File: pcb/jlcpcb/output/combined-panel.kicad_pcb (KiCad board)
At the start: 2 copper layers, 138.8 x 150.1 mm, 163 parts, among them J101 B12B-PHDSS, J201 Conn_01x06_MountingPin, J202 B12B-PHDSS, SW10 SW_Push, SW11 SW_Push, SW12 SW_Push, SW13 SW_Push, SW15 SW_Push, SW16 SW_Push, SW17 SW_Push, SW18 SW_Push, SW19 SW_Push, SW20 SW_Push, SW22 SW_Push, SW23 SW_Push, SW24 SW_Push, SW25 SW_Push, SW26 SW_Push, SW27 SW_Push, SW28 SW_Push, SW29 SW_Push, SW30 SW_Push, SW31 SW_Push, SW32 SW_Push, SW33 SW_Push, SW34 SW_Push, SW35 SW_Push, SW43 SW_Push, SW44 SW_Push, SW45 SW_Push, SW46 SW_Push, SW47 SW_Push, SW48 SW_Push, SW50 SW_Push, SW51 SW_Push, SW52 SW_Push, SW53 SW_Push, SW54 SW_Push, SW55 SW_Push, SW57 SW_Push, SW58 SW_Push, SW59 SW_Push, SW60 SW_Push, SW61 SW_Push, SW62 SW_Push, SW63 SW_Push, SW64 SW_Push, SW65 SW_Push, SW69 SW_Push, SW70 SW_Push, SW8 SW_Push, SW9 SW_Push, U201 XIAO nRF52840 Plus

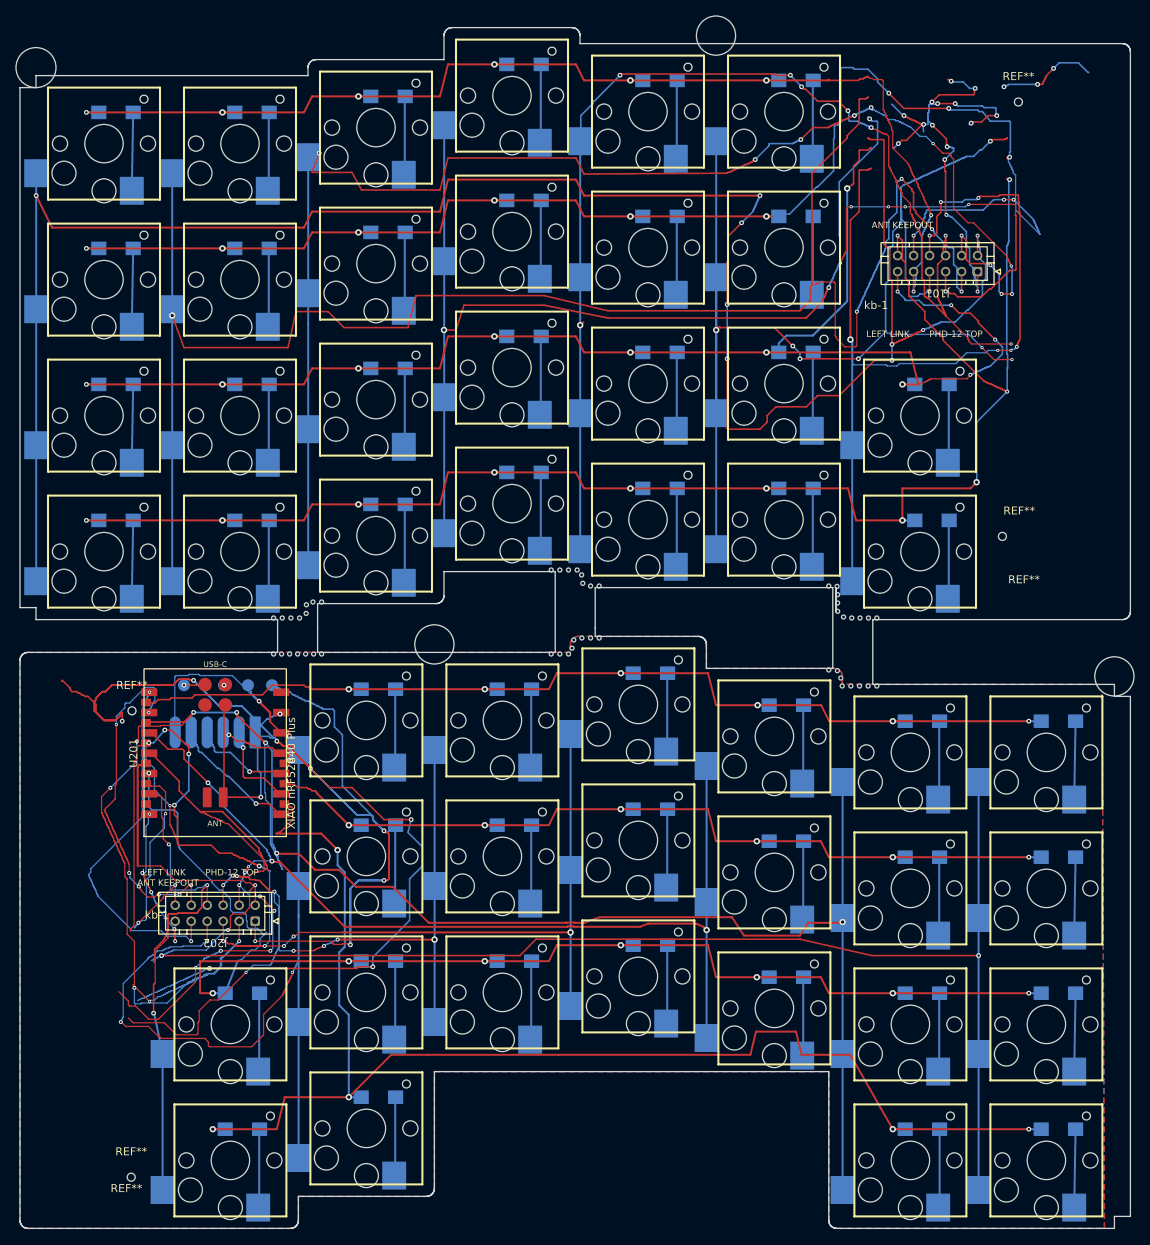
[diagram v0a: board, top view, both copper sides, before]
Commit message: Replace split connectors with Samtec FFSD-compatible headers
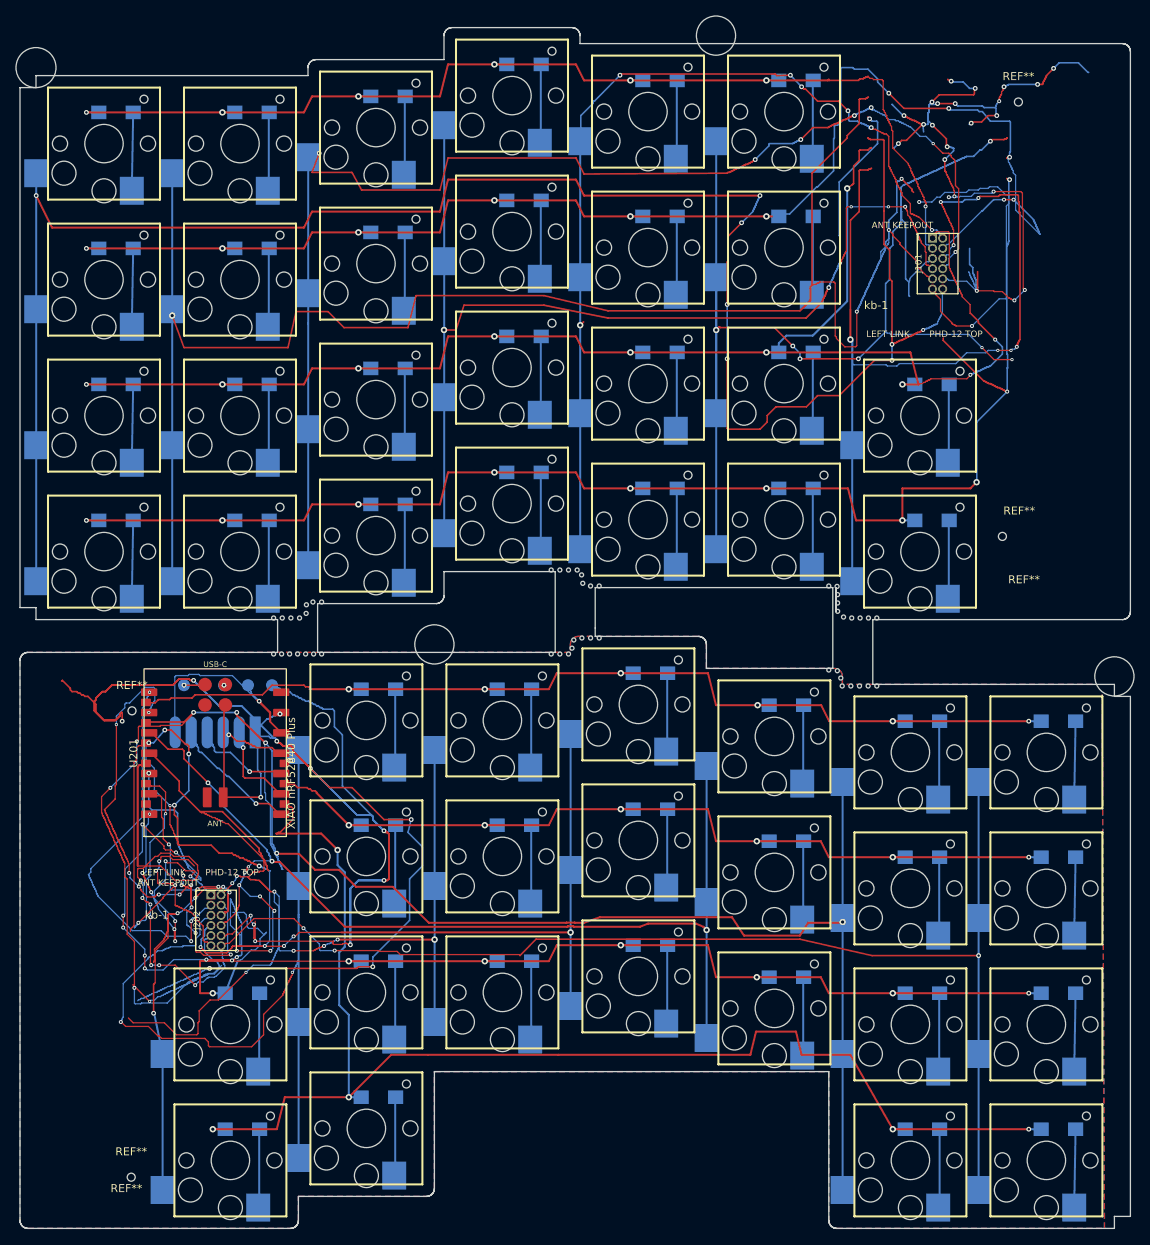
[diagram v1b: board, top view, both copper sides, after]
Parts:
- J101, J202: value B12B-PHDSS -> FTSH-106-01-L-D-K; footprint Connector_JST:JST_PHD_B12B-PHDSS_2x06_P2.00mm_Vertical -> Library:Samtec_FTSH-106-01-L-D-K
- moved J101 7.01 mm to (144.7, 39.3), turned to 0 degrees
- moved J202 6.43 mm to (54.5, 121.4), turned to 0 degrees
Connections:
- J101 pad 1: Board_0-GND -> Board_0-/left/LROW2
- J101 pad 10: Board_0-/left/LROW1 -> Board_0-GND
- J101 pad 11: Board_0-/left/LROW2 -> Board_0-/left/LROW3
- J101 pad 12: Board_0-/left/LROW3 -> Board_0-/left/COL0
- J101 pad 2: Board_0-/left/COL0 -> Board_0-/left/COL4
- J101 pad 3: Board_0-/left/COL1 -> Board_0-/left/LROW0
- J101 pad 4: Board_0-/left/COL2 -> Board_0-/left/LROW1
- J101 pad 5: Board_0-/left/COL3 -> Board_0-/left/COL5
- J101 pad 6: Board_0-/left/COL4 -> Board_0-/left/COL6
- J101 pad 7: Board_0-/left/COL5 -> Board_0-/left/COL3
- J101 pad 8: Board_0-/left/COL6 -> Board_0-/left/COL2
- J101 pad 9: Board_0-/left/LROW0 -> Board_0-/left/COL1
- J202 pad 1: Board_1-GND -> Board_1-/right/LROW2
- J202 pad 10: Board_1-/right/LROW1 -> Board_1-GND
- J202 pad 11: Board_1-/right/LROW2 -> Board_1-/right/LROW3
- J202 pad 12: Board_1-/right/LROW3 -> Board_1-/right/COL0
- J202 pad 2: Board_1-/right/COL0 -> Board_1-/right/COL4
- J202 pad 3: Board_1-/right/COL1 -> Board_1-/right/LROW0
- J202 pad 4: Board_1-/right/COL2 -> Board_1-/right/LROW1
- J202 pad 5: Board_1-/right/COL3 -> Board_1-/right/COL5
- J202 pad 6: Board_1-/right/COL4 -> Board_1-/right/COL6
- J202 pad 7: Board_1-/right/COL5 -> Board_1-/right/COL3
- J202 pad 8: Board_1-/right/COL6 -> Board_1-/right/COL2
- J202 pad 9: Board_1-/right/LROW0 -> Board_1-/right/COL1
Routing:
- net Board_1-/right/RROW2: track 165.4 -> 224.0 mm, vias 8 -> 17
- net Board_0-GND: track 81.7 -> 114.6 mm, vias 18 -> 23
- net Board_0-/left/COL4: track 148.7 -> 116.1 mm, vias 8 -> 7
- net Board_0-/left/COL3: track 178.4 -> 152.6 mm, vias 9 -> 7
- net Board_1-/right/LROW1: track 44.0 -> 67.6 mm, vias 7 -> 12
- net Board_0-/left/LROW3: track 204.0 -> 225.4 mm, vias 11 -> 12
- net Board_0-/left/COL2: track 182.8 -> 162.9 mm, vias 11 -> 7
- net Board_1-/right/LROW3: track 31.6 -> 50.1 mm, vias 3 -> 5
- net Board_1-/right/LROW2: track 20.5 -> 38.4 mm, vias 5 -> 8
- net Board_1-/right/COL2: track 160.8 -> 143.5 mm, vias 11 -> 10
- net Board_0-/left/COL0: track 259.5 -> 246.5 mm, vias 9 -> 8
- net Board_1-/right/COL3: track 168.0 -> 178.9 mm
- net Board_1-/right/COL4: track 154.1 -> 145.3 mm, vias 9 -> 8
- net Board_0-/left/LROW0: track 147.3 -> 138.8 mm, vias 8 -> 7
- net Board_1-GND: track 319.0 -> 327.2 mm, vias 13 -> 15
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
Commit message: Shrink inner edges of split PCBs
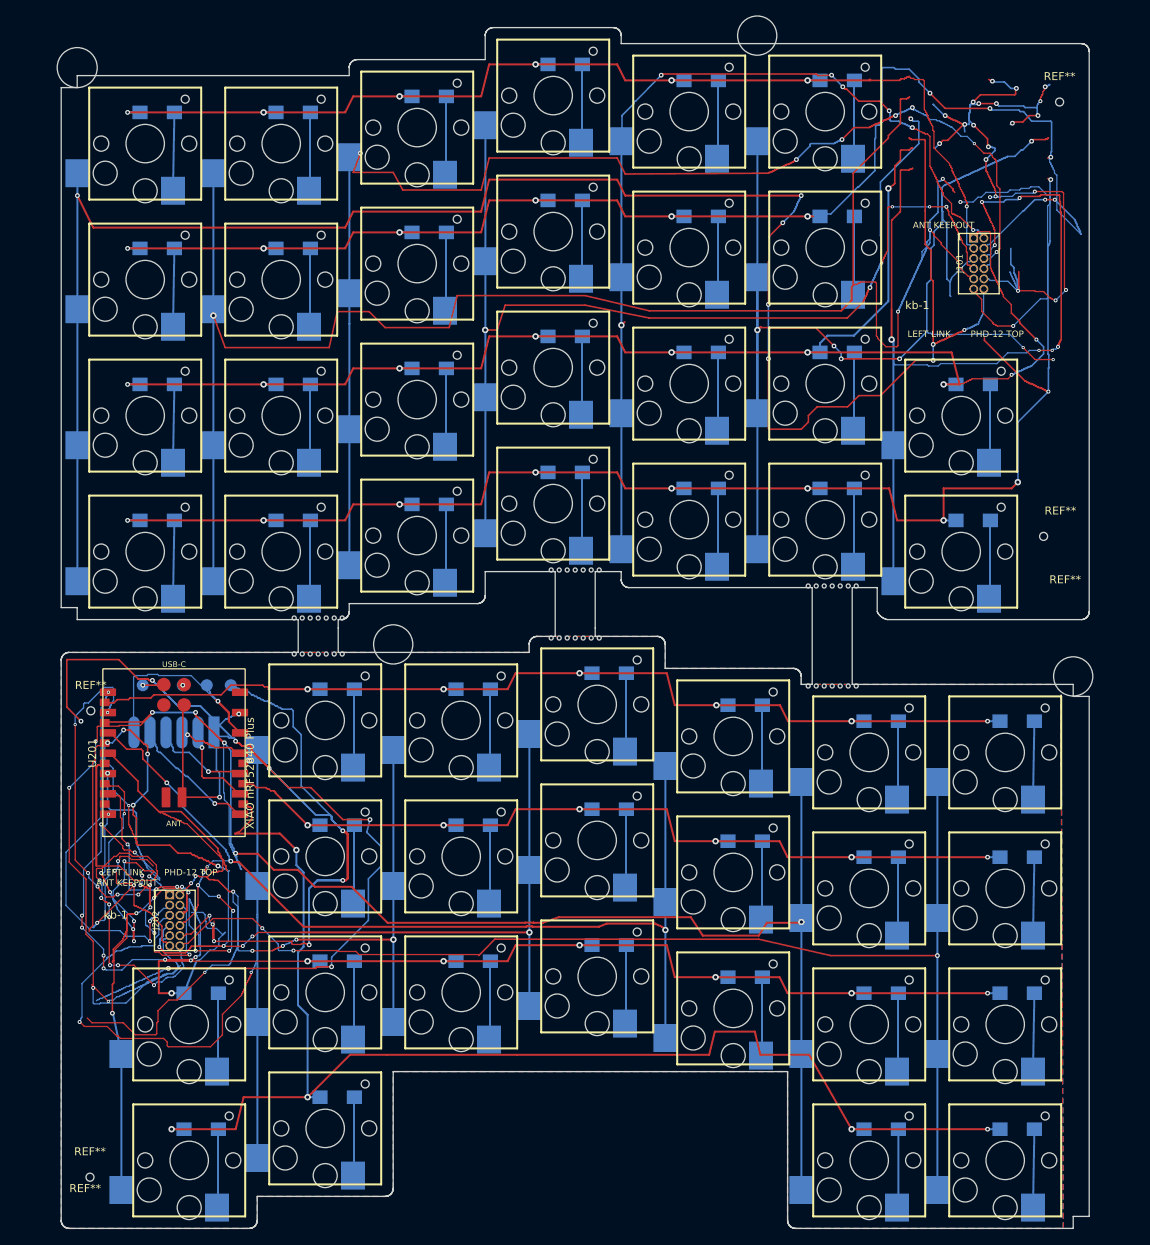
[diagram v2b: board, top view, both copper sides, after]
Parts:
- removed KiKit_MB_1_8, KiKit_MB_2_8, KiKit_MB_3_10, KiKit_MB_3_8, KiKit_MB_3_9, KiKit_MB_5_8, KiKit_MB_6_8: NPTH, NPTH
- removed the REF** at (32.6, 18.0)
- removed the REF** at (117.6, 14.0)
- removed the REF** at (82.4, 90.1)
- removed the REF** at (44.5, 156.7)
- removed the REF** at (167.4, 94.1)
- removed the REF** at (44.6, 98.4)
- removed the REF** at (155.4, 22.3)
- removed the REF** at (155.5, 76.6)
- added REF**: MountingHole_5mm, Library:MountingHole_5mm, F.Cu at (122.8, 14.0)
- added REF**: Hole_1mm, Library:Hole_1mm, F.Cu at (160.7, 76.6)
- added REF**: Hole_1mm, Library:Hole_1mm, F.Cu at (39.5, 98.4)
- added REF**: MountingHole_5mm, Library:MountingHole_5mm, F.Cu at (77.2, 90.1)
- added REF**: Hole_1mm, Library:Hole_1mm, F.Cu at (160.6, 22.3)
- added REF**: MountingHole_5mm, Library:MountingHole_5mm, F.Cu at (37.8, 18.0)
- added REF**: MountingHole_5mm, Library:MountingHole_5mm, F.Cu at (162.2, 94.1)
- added REF**: Hole_1mm, Library:Hole_1mm, F.Cu at (39.4, 156.7)
- moved D10 5.15 mm to (81.8, 21.6)
- moved D11 5.15 mm to (98.8, 17.6)
- moved D12 5.15 mm to (115.8, 19.6)
- moved D13 5.15 mm to (132.8, 19.6)
- moved D17 5.15 mm to (81.8, 38.6)
- moved D18 5.15 mm to (98.8, 34.6)
- moved D19 5.15 mm to (115.8, 36.6)
- moved D20 5.15 mm to (132.8, 36.6)
- moved D24 5.15 mm to (81.8, 55.6)
- moved D25 5.15 mm to (98.8, 51.6)
- moved D26 5.15 mm to (115.8, 53.6)
- moved D27 5.15 mm to (132.8, 53.6)
- moved D28 5.15 mm to (149.8, 57.6)
- moved D31 5.15 mm to (81.8, 72.6)
- moved D32 5.15 mm to (98.8, 68.6)
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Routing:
- net Board_1-GND: track 327.2 -> 298.3 mm
- net Board_0-GND: track 114.6 -> 102.6 mm, vias 23 -> 21
- net Board_1-/right/LROW0: track 49.2 -> 47.2 mm
- net Board_1-/right/LROW1: track 67.6 -> 66.3 mm
- net Board_1-/right/COL1: track 267.0 -> 266.1 mm
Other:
- board size 138.8 x 150.1 mm -> 128.5 x 150.1 mm

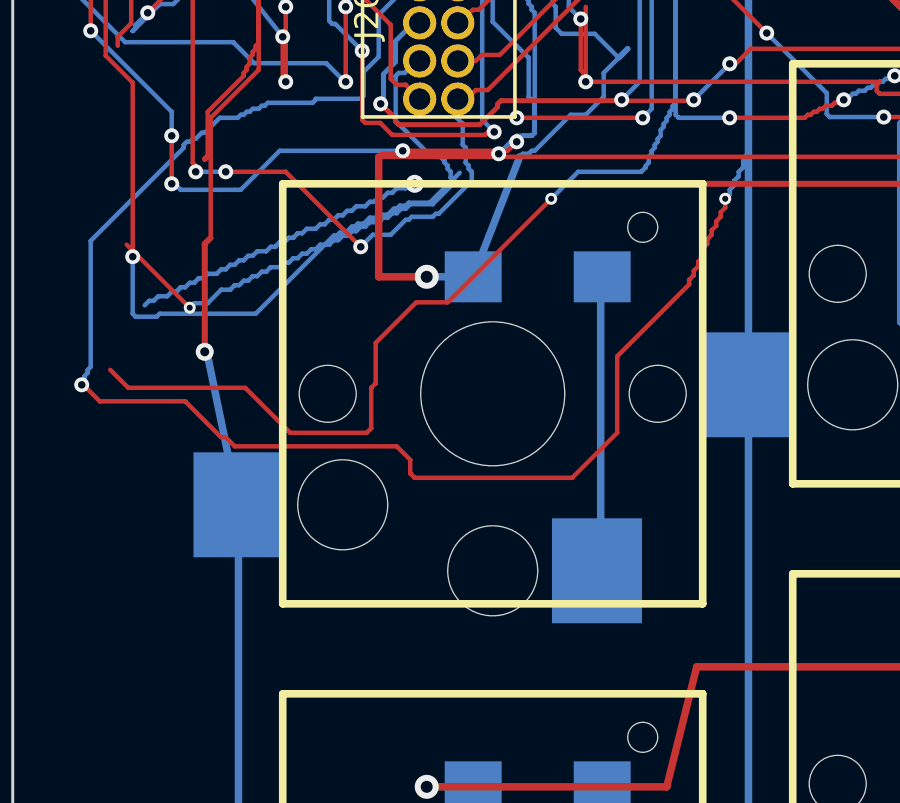
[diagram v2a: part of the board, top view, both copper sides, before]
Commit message: Remove key below right split connector
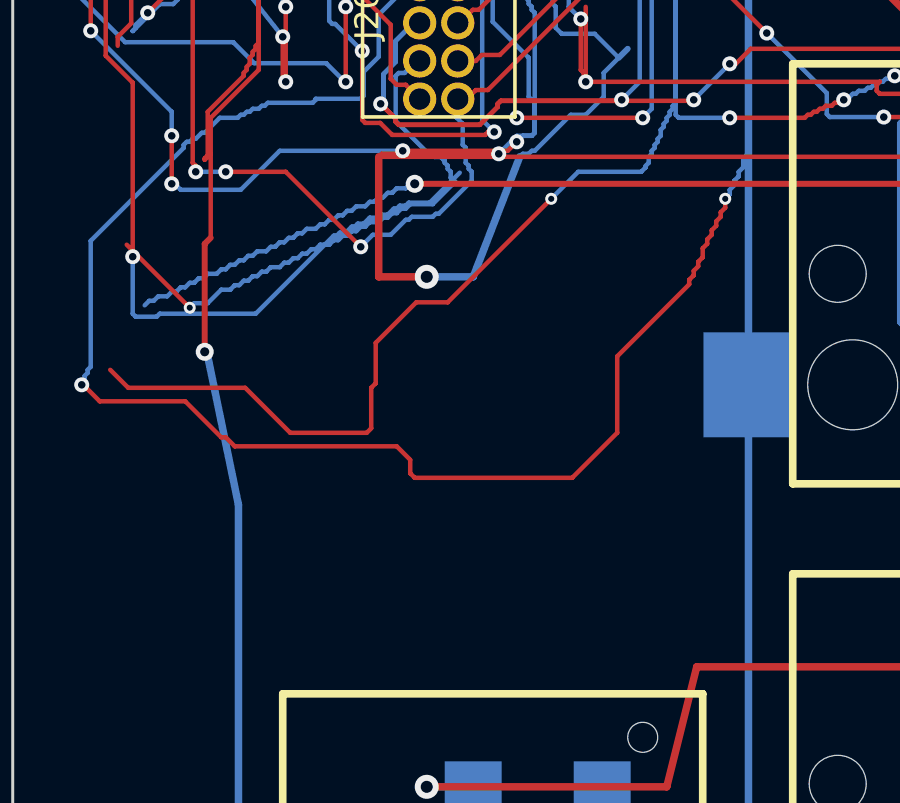
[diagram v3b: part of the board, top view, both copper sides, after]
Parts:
- removed D63: 1N4148W, Library:D_SOD-123_HandSoldering
- removed SW63: SW_Push, Library:CHOC_V2_SOCKET_HANDSOLDERING_17mm
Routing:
- net Board_1-Net-(D63-K): track 9.87 -> 0.00 mm
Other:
- board text removed: "D63"
- board text removed: "SW63"

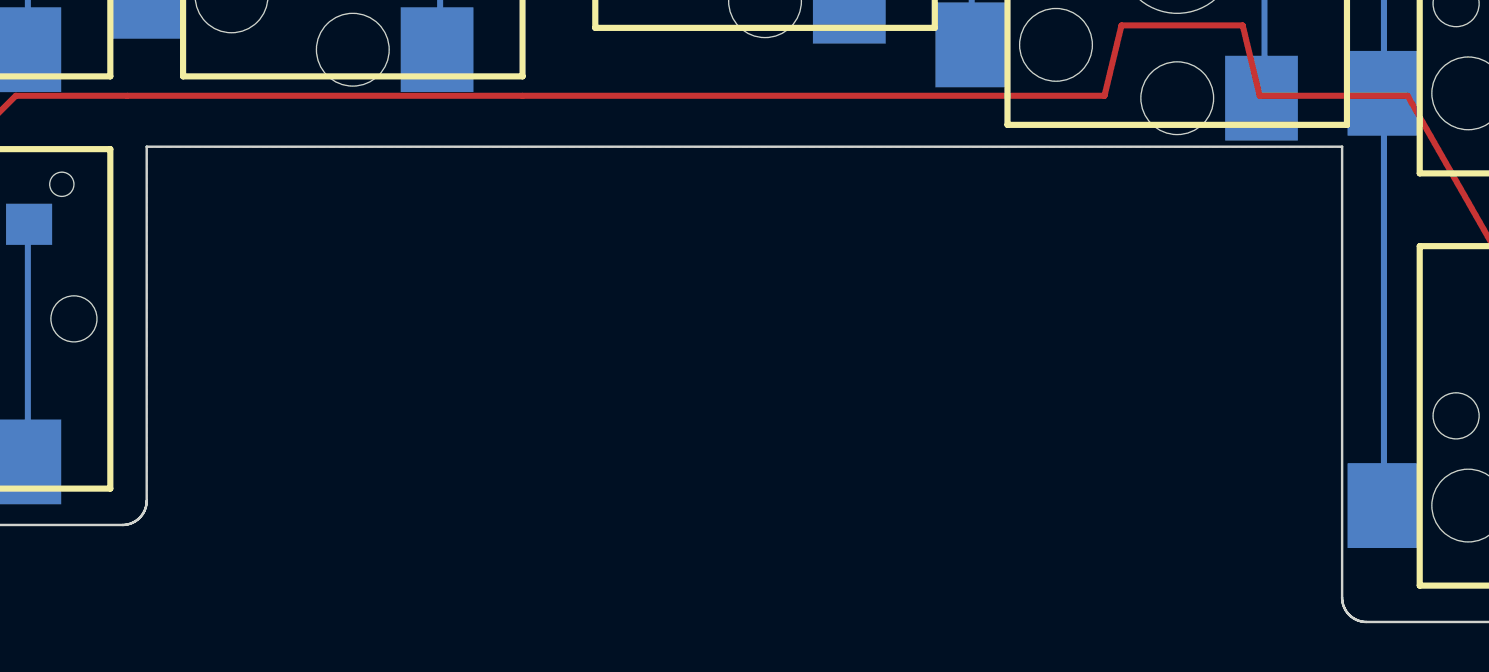
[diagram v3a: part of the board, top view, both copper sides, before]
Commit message: Fit right PCB outline around inner key
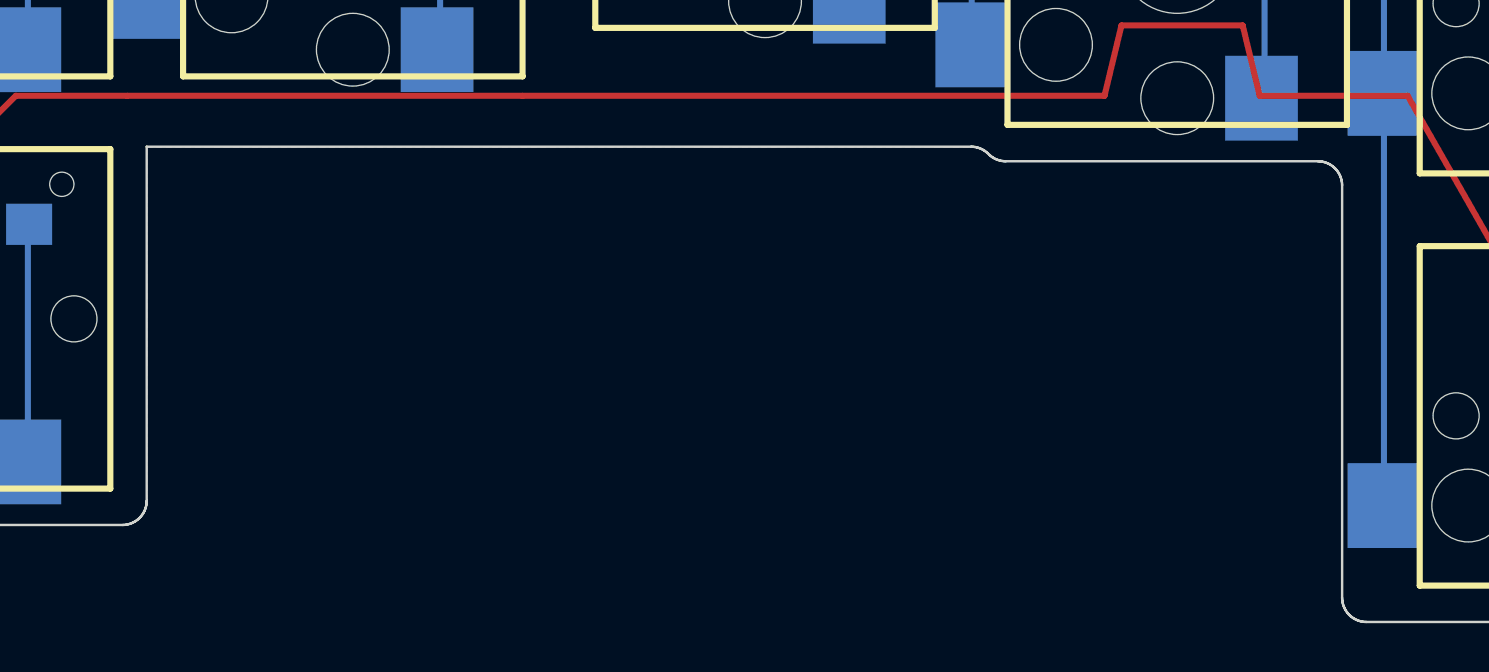
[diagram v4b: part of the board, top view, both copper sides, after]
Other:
- outline, holes or cut-outs redrawn
